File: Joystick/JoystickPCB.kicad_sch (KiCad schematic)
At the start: 19 parts, among them J1 JST B6B-PH-SM4-TB, J2 JST B4B-PH-SM4-TB, J3 JST B4B-PH-SM4-TB, J4 JST B3B-PH-SM4-TB, U1 MIC5225-1.8YM5-TR, U2 ADS1115IDGSR, U3 ICM-20948

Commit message: Delted Altium verison and added some manufacturer part numbers (still need to do R and C)
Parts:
- J1: Manufacturer Part Number (none) -> B6B-PH-SM4-TB
- J2, J3: Manufacturer Part Number (none) -> B4B-PH-SM4-TB
- J4: Manufacturer Part Number (none) -> B3B-PH-SM4-TB
- Q1: Manufacturer Part Number (none) -> BSS138BKS,115
- U1: Manufacturer Part Number (none) -> MIC5225-1.8YM5-TR
- U2: Manufacturer Part Number (none) -> ADS1115IDGSR
- U3: Manufacturer Part Number (none) -> ICM-20948

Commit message: Changed R and C sizes and added part numbers
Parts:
- C1, C2, C4: Manufacturer Part Number (none) -> GRM21BR61C106KE15K
- C3, C5: footprint Capacitor_SMD:C_0603_1608Metric -> Capacitor_SMD:C_0805_2012Metric; Manufacturer Part Number (none) -> CC0805KRX7R9BB104
- R1, R2: footprint Resistor_SMD:R_0603_1608Metric -> Resistor_SMD:R_0805_2012Metric; Manufacturer Part Number (none) -> CRCW08054K70FKEAC
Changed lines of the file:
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@@
 			)
 		)
-		(property "Footprint" "Capacitor_SMD:C_0603_1608Metric"
+		(property "Footprint" "Capacitor_SMD:C_0805_2012Metric"
 			(at 111.4552 36.83 0)
 			(effects
@@
 			)
 		)
-		(property "Manufacturer Part Number" ""
+		(property "Manufacturer Part Number" "CC0805KRX7R9BB104"
 			(at 110.49 33.02 0)
 			(effects
@@
 			)
 		)
-		(property "Footprint" "Capacitor_SMD:C_0603_1608Metric"
+		(property "Footprint" "Capacitor_SMD:C_0805_2012Metric"
 			(at 249.8852 72.39 0)
 			(effects
@@
 			)
 		)
-		(property "Manufacturer Part Number" ""
+		(property "Manufacturer Part Number" "CC0805KRX7R9BB104"
 			(at 248.92 68.58 0)
 			(effects
@@
 			)
 		)
-		(property "Footprint" "Resistor_SMD:R_0603_1608Metric"
+		(property "Footprint" "Resistor_SMD:R_0805_2012Metric"
 			(at 151.892 63.5 90)
 			(effects
@@
 			)
 		)
-		(property "Manufacturer Part Number" ""
+		(property "Manufacturer Part Number" "CRCW08054K70FKEAC"
 			(at 153.67 63.5 0)
 			(effects
@@
 			)
 		)
-		(property "Manufacturer Part Number" ""
+		(property "Manufacturer Part Number" "GRM21BR61C106KE15K"
 			(at 246.38 114.3 0)
 			(effects
@@
 			)
 		)
-		(property "Footprint" "Resistor_SMD:R_0603_1608Metric"
+		(property "Footprint" "Resistor_SMD:R_0805_2012Metric"
 			(at 151.892 29.21 90)
 			(effects
@@
 			)
 		)
-		(property "Manufacturer Part Number" ""
+		(property "Manufacturer Part Number" "CRCW08054K70FKEAC"
 			(at 153.67 29.21 0)
 			(effects
@@
 			)
 		)
-		(property "Manufacturer Part Number" ""
+		(property "Manufacturer Part Number" "GRM21BR61C106KE15K"
 			(at 97.79 33.02 0)
 			(effects
@@
 			)
 		)
-		(property "Manufacturer Part Number" ""
+		(property "Manufacturer Part Number" "GRM21BR61C106KE15K"
 			(at 24.13 35.56 0)
 			(effects

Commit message: Switch mounting holes to M3 ISO 7380
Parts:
- H1, H2, H3, H4: footprint MountingHole:MountingHole_3.2mm_M3_DIN965_Pad_TopBottom -> MountingHole:MountingHole_3.2mm_M3_ISO7380_Pad
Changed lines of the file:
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@@
 			)
 		)
-		(property "Footprint" "MountingHole:MountingHole_3.2mm_M3_DIN965_Pad_TopBottom"
+		(property "Footprint" "MountingHole:MountingHole_3.2mm_M3_ISO7380_Pad"
 			(at 22.86 80.01 0)
 			(effects
@@
 			)
 		)
-		(property "Footprint" "MountingHole:MountingHole_3.2mm_M3_DIN965_Pad_TopBottom"
+		(property "Footprint" "MountingHole:MountingHole_3.2mm_M3_ISO7380_Pad"
 			(at 22.86 69.85 0)
 			(effects
@@
 			)
 		)
-		(property "Footprint" "MountingHole:MountingHole_3.2mm_M3_DIN965_Pad_TopBottom"
+		(property "Footprint" "MountingHole:MountingHole_3.2mm_M3_ISO7380_Pad"
 			(at 43.18 69.85 0)
 			(effects
@@
 			)
 		)
-		(property "Footprint" "MountingHole:MountingHole_3.2mm_M3_DIN965_Pad_TopBottom"
+		(property "Footprint" "MountingHole:MountingHole_3.2mm_M3_ISO7380_Pad"
 			(at 43.18 81.28 0)
 			(effects

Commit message: Fixed mounting holes positions and general board cleanup
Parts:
- U2: footprint Library:SOP50P490X110-10N -> Package_SO:VSSOP-10_3x3mm_P0.5mm
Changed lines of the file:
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@@
 			)
 		)
-		(property "Footprint" "Library:SOP50P490X110-10N"
+		(property "Footprint" "Package_SO:VSSOP-10_3x3mm_P0.5mm"
 			(at 222.25 124.46 0)
 			(effects

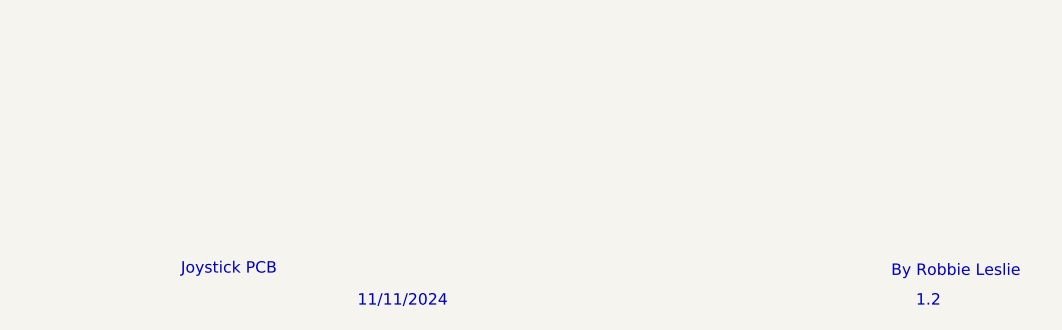
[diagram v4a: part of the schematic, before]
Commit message: Swapped microcontroller connector for horizontal one
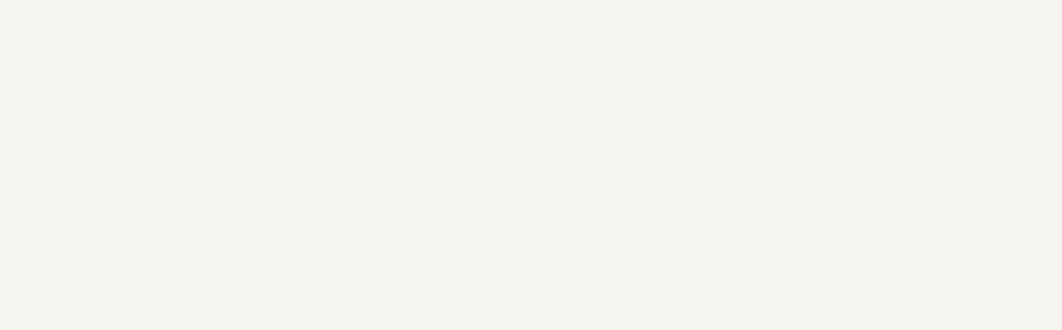
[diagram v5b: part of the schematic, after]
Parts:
- J1: footprint Connector_JST:JST_PH_B6B-PH-SM4-TB_1x06-1MP_P2.00mm_Vertical -> Connector_JST:JST_PH_S6B-PH-SM4-TB_1x06-1MP_P2.00mm_Horizontal; Manufacturer Part Number B6B-PH-SM4-TB -> S6B-PH-SM4-TB
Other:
- note removed: "1.2"
- note removed: "11/11/2024"
- note removed: "By Robbie Leslie"
- note removed: "Joystick PCB"
- company: (none) -> Lafayette College
- title: (none) -> Joystick and IMU Board
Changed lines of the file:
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@@
 	(generator_version "8.0")
 	(paper "A4")
+	(title_block
+		(title "Joystick and IMU Board")
+		(date "2025-02-11")
+		(rev "v1.0")
+		(company "Lafayette College")
+		(comment 1 "By Robbie Leslie")
+	)
 	(junction
 		(at 97.79 29.21)
@@
 		)
 	)
-	(text "1.2"
-		(exclude_from_sim no)
-		(at 271.018 193.294 0)
-		(effects
-			(font
-				(size 1.27 1.27)
-			)
-		)
-	)
-	(text "11/11/2024\n"
-		(exclude_from_sim no)
-		(at 212.598 193.294 0)
-		(effects
-			(font
-				(size 1.27 1.27)
-			)
-		)
-	)
 	(text "To Fingerprint Sensor"
 		(exclude_from_sim no)
@@
 		)
 	)
-	(text "Joystick PCB"
-		(exclude_from_sim no)
-		(at 193.294 189.738 0)
-		(effects
-			(font
-				(size 1.27 1.27)
-			)
-		)
-	)
 	(text "To Pico"
 		(exclude_from_sim no)
@@
 		(exclude_from_sim no)
 		(at 221.742 98.552 0)
-		(effects
-			(font
-				(size 1.27 1.27)
-			)
-		)
-	)
-	(text "By Robbie Leslie"
-		(exclude_from_sim no)
-		(at 274.066 189.992 0)
 		(effects
 			(font
@@
 			)
 		)
-		(property "Footprint" "Connector_JST:JST_PH_B6B-PH-SM4-TB_1x06-1MP_P2.00mm_Vertical"
+		(property "Footprint" "Connector_JST:JST_PH_S6B-PH-SM4-TB_1x06-1MP_P2.00mm_Horizontal"
 			(at 43.18 133.35 0)
 			(effects
@@
 			)
 		)
-		(property "Manufacturer Part Number" "B6B-PH-SM4-TB"
+		(property "Manufacturer Part Number" "S6B-PH-SM4-TB"
 			(at 43.18 133.35 0)
 			(effects

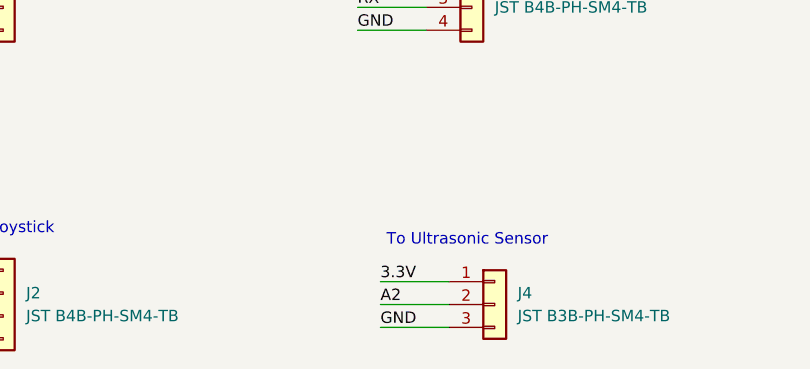
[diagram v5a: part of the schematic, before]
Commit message: Updated ultrasonic header connection to match with sensor pinout
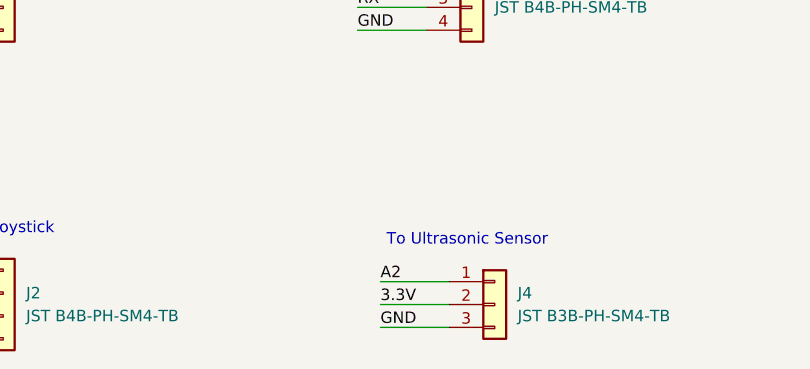
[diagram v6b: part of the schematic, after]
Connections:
- net 3.3V: now also J4.2 (Pin_2); no longer J4.1 (Pin_1)
- net A2: now also J4.1 (Pin_1); no longer J4.2 (Pin_2)
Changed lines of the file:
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@@
+		)
+	)
+	(label "A2"
+		(at 85.09 168.91 0)
+		(effects
+			(font
+				(size 1.27 1.27)
+			)
+			(justify left bottom)
 		)
 	)
@@
 		)
 	)
+	(label "3.3V"
+		(at 85.09 171.45 0)
+		(effects
+			(font
+				(size 1.27 1.27)
+			)
+			(justify left bottom)
+		)
+	)
 	(label "A0"
 		(at 30.48 172.72 0)
@@
 	(label "3.3V"
 		(at 29.21 130.81 0)
-		(effects
-			(font
-				(size 1.27 1.27)
-			)
-			(justify left bottom)
-		)
-	)
-	(label "A2"
-		(at 85.09 171.45 0)
 		(effects
 			(font
@@
 		(effects
 			(font
-				(size 1.27 1.27)
-			)
-			(justify left bottom)
-		)
-	)
-	(label "3.3V"
-		(at 85.09 168.91 0)
-		(effects
-			(font
